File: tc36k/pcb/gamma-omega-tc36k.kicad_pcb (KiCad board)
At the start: 2 copper layers, 232.8 x 111.4 mm, 45 parts

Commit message: Fix C9
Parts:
- moved S36 0.43 mm to (194.7, 146.4)
- moved S16 0.43 mm to (88.0, 122.3)
- moved S22 0.43 mm to (244.9, 94.2)
- moved S21 0.43 mm to (264.2, 68.2)
- moved H5 0.43 mm to (132.9, 56.4)
- moved S28 0.43 mm to (210.4, 105.7)
- moved S33 0.43 mm to (182.6, 84.7)
- moved S19 0.43 mm to (264.2, 102.2)
- moved H3 0.43 mm to (43.9, 115.9)
- moved S26 0.43 mm to (219.9, 76.0)
- moved S13 0.43 mm to (119.8, 116.2)
- moved S1 0.43 mm to (50.9, 102.2)
- moved S3 0.43 mm to (50.9, 68.2)
- moved S5 0.43 mm to (73.1, 77.4)
- moved S12 0.43 mm to (117.4, 74.2)
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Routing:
- net C9: track 118.6 -> 125.4 mm

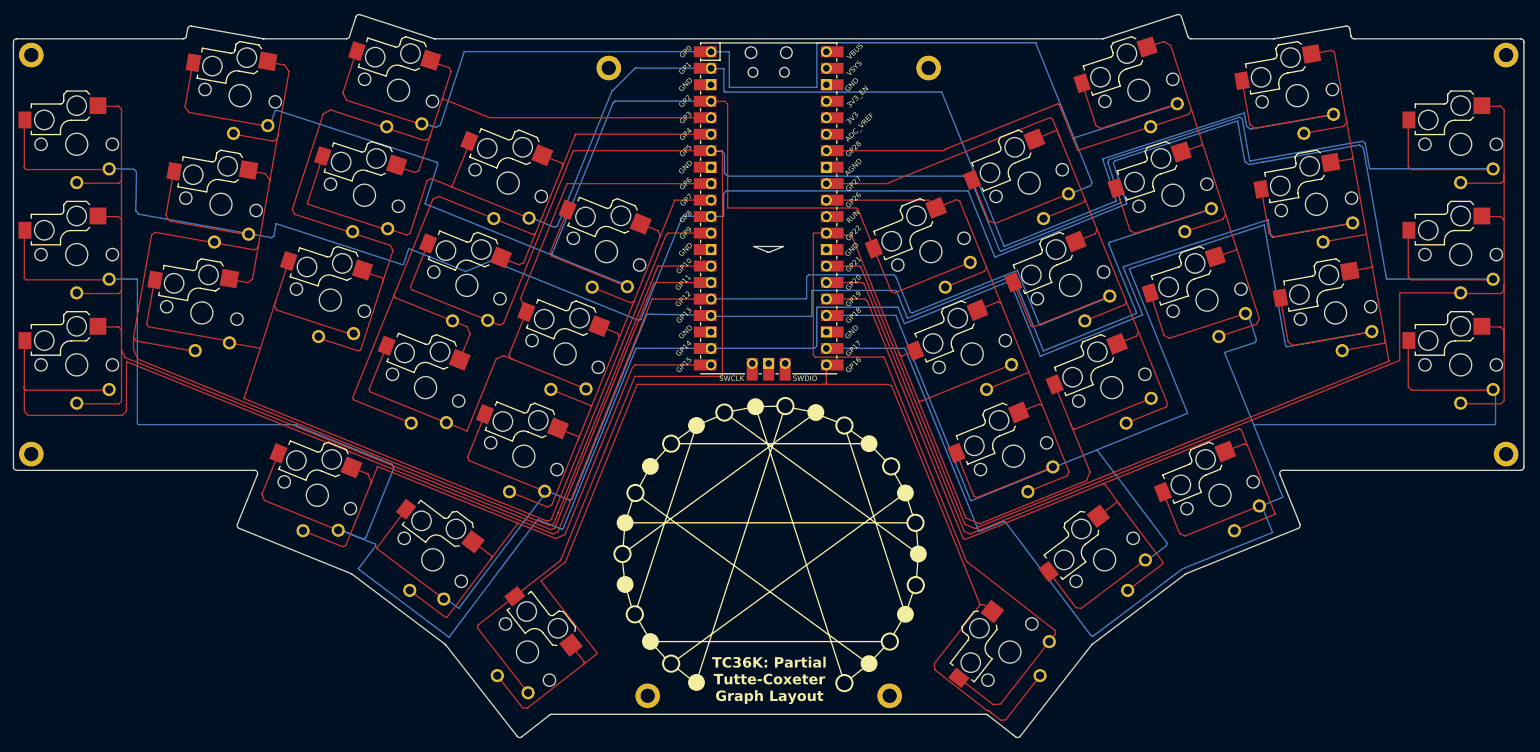
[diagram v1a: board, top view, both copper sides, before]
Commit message: Fix R2, C1 left ring, C10 right pinky etc trace margins
This was a relic of an early copy-paste positioning.
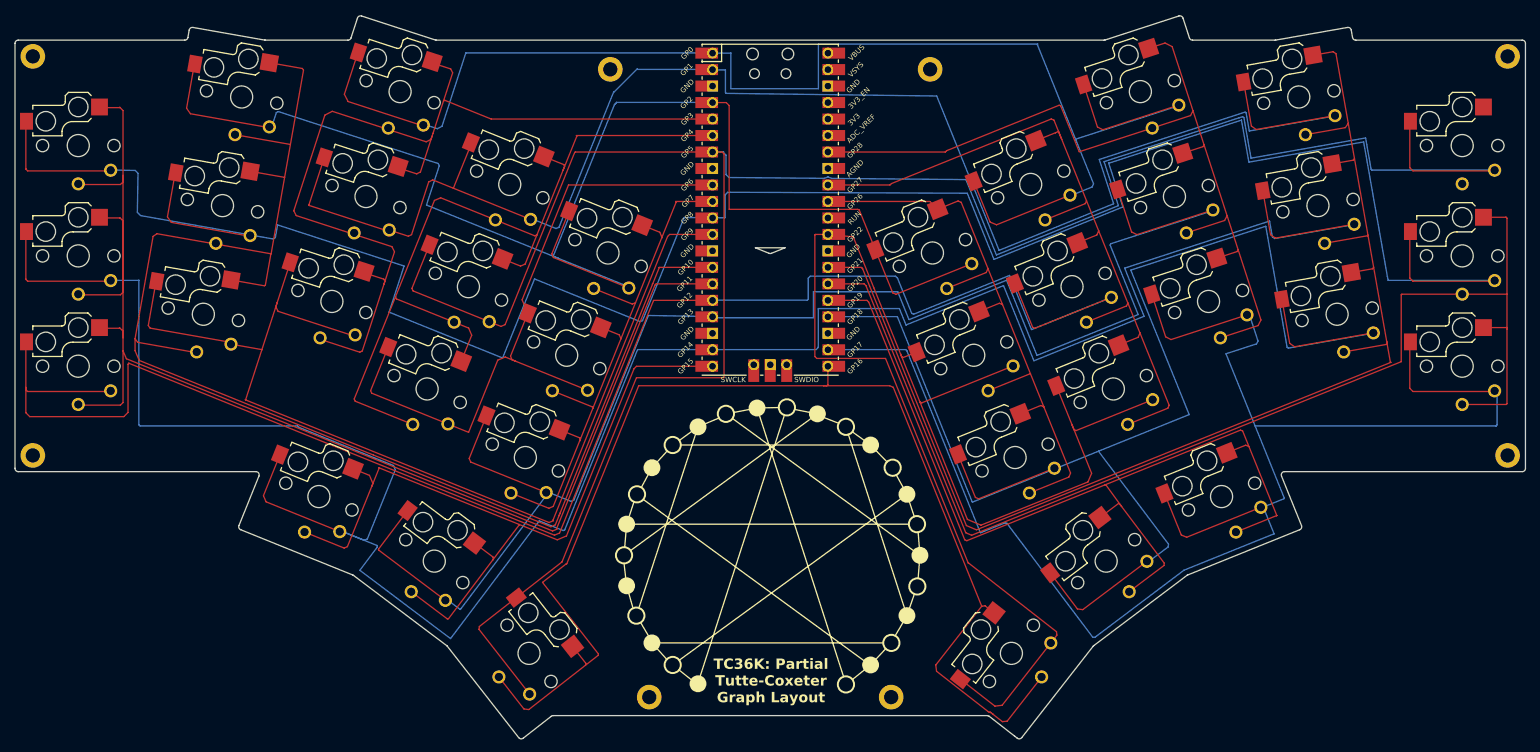
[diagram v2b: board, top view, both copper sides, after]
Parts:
- moved S3 0.31 mm to (51.1, 68.4)
- moved H3 0.31 mm to (44.1, 116.1)
- moved H6 0.31 mm to (182.4, 56.6)
- moved S36 0.31 mm to (195.0, 146.6)
- moved S30 0.31 mm to (197.9, 74.4)
- moved H8 0.31 mm to (176.4, 153.4)
- moved S1 0.31 mm to (51.1, 102.4)
- moved S35 0.31 mm to (209.6, 132.4)
- moved S32 0.31 mm to (189.2, 100.7)
- moved S18 0.31 mm to (120.6, 146.6)
- moved S8 0.31 mm to (95.5, 76.2)
- moved S29 0.31 mm to (204.3, 90.1)
- moved S19 0.31 mm to (264.4, 102.4)
- moved H2 0.31 mm to (271.4, 54.6)
- moved S16 0.31 mm to (88.2, 122.5)
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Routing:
- net C12: track 221.6 -> 189.2 mm
- net R2: track 343.7 -> 361.0 mm
- net C2: track 219.7 -> 227.2 mm
- net R13: track 358.8 -> 360.1 mm
- net R4: track 250.4 -> 251.4 mm
